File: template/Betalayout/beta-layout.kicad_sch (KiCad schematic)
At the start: 0 parts

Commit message: Update footprint for SMD capacitor and crystals
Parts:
- added CN1: GSB343K331HR, User_Github:GSB343K331HR, symbol User:GSB343K331HR
- added R1: 1K, symbol User:R
- added U1: LM1117IMPX-3.3/NOPB, User:LM1117IMPX-3.3NOPB, symbol User:LM1117IMPX-3.3/NOPB
- added U2: STM32F103C8T6, User:STM32F103C8T6, symbol User:STM32F103C8T6

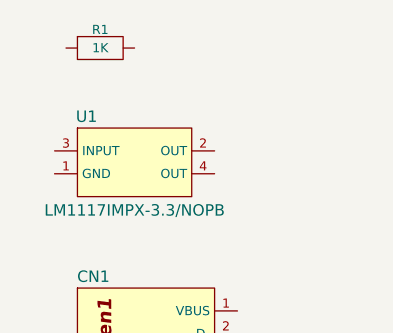
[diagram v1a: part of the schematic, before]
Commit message: Add footprint for SMD LED
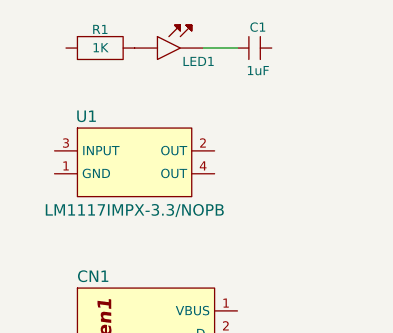
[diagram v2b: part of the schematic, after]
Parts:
- added C1: 1uF, symbol User:C
- added LED1: ~, symbol User:LED
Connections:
- net at R1.2: now also LED1.1
- new net: C1.1, LED1.2
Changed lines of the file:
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@@
 		(comment 1 "Zhangshun Lu")
+	)
+	(wire
+		(pts
+			(xy 38.1 25.4) (xy 34.29 25.4)
+		)
+		(stroke
+			(width 0)
+			(type default)
+		)
 	)
 	(symbol
@@
 	)
 	(symbol
+		(lib_id "User:LED")
+		(at 30.48 25.4 0)
+		(unit 1)
+		(exclude_from_sim no)
+		(in_bom yes)
+		(on_board yes)
+		(dnp no)
+		(fields_autoplaced yes)
+		(property "Reference" "LED1"
+			(at 33.782 26.924 0)
+			(do_not_autoplace yes)
+			(effects
+				(font
+					(size 1.016 1.016)
+				)
+			)
+		)
+		(property "Value" "~"
+			(at 30.48 25.4 0)
+			(do_not_autoplace yes)
+			(effects
+				(font
+					(size 1.016 1.016)
+					(color 64 55 255 1)
+				)
+				(hide yes)
+			)
+		)
+		(property "Footprint" ""
+			(at 30.48 25.4 0)
+			(effects
+				(font
+					(size 1.27 1.27)
+				)
+				(hide yes)
+			)
+		)
+		(property "Datasheet" ""
+			(at 30.48 25.4 0)
+			(effects
+				(font
+					(size 1.27 1.27)
+				)
+				(hide yes)
+			)
+		)
+		(property "Description" "LED"
+			(at 30.48 25.4 0)
+			(effects
+				(font
+					(size 1.27 1.27)
+				)
+				(hide yes)
+			)
+		)
+		(property "MPN" ""
+			(at 30.48 25.4 0)
+			(effects
+				(font
+					(size 1.016 1.016)
+				)
+				(hide yes)
+			)
+		)
+		(property "Manufacturer" ""
+			(at 30.48 25.4 0)
+			(effects
+				(font
+					(size 1.016 1.016)
+				)
+				(hide yes)
+			)
+		)
+		(pin "2"
+		)
+		(pin "1"
+		)
+		(instances
+			(project ""
+				(path "/695d78a6-3e90-439f-9889-ee1335c900cb"
+					(reference "LED1")
+					(unit 1)
+				)
+			)
+		)
+	)
+	(symbol
 		(lib_id "User:GSB343K331HR")
 		(at 27.94 49.53 0)
@@
 					(unit 1)
 				)
+			)
+		)
+	)
+	(symbol
+		(lib_id "User:C")
+		(at 40.64 25.4 0)
+		(unit 1)
+		(exclude_from_sim no)
+		(in_bom yes)
+		(on_board yes)
+		(dnp no)
+		(fields_autoplaced yes)
+		(property "Reference" "C1"
+			(at 40.386 23.114 0)
+			(do_not_autoplace yes)
+			(effects
+				(font
+					(size 1.016 1.016)
+				)
+			)
+		)
+		(property "Value" "1uF"
+			(at 40.386 27.94 0)
+			(do_not_autoplace yes)
+			(effects
+				(font
+					(size 1.016 1.016)
+					(color 64 55 255 1)
+				)
+			)
+		)
+		(property "Footprint" ""
+			(at 40.64 25.4 0)
+			(effects
+				(font
+					(size 1.27 1.27)
+				)
+				(hide yes)
+			)
+		)
+		(property "Datasheet" ""
+			(at 40.64 25.4 0)
+			(effects
+				(font
+					(size 1.27 1.27)
+				)
+				(hide yes)
+			)
+		)
+		(property "Description" "Capacitor"
+			(at 40.64 25.4 0)
+			(effects
+				(font
+					(size 1.27 1.27)
+				)
+				(hide yes)
+			)
+		)
+		(property "MPN" ""
+			(at 40.64 25.4 0)
+			(effects
+				(font
+					(size 1.016 1.016)
+				)
+				(hide yes)
+			)
+		)
+		(property "Manufacturer" ""
+			(at 40.64 25.4 0)
+			(effects
+				(font
+					(size 1.016 1.016)
+				)
+				(hide yes)
+			)
+		)
+		(pin "1"
+		)
+		(pin "2"
+		)
+		(instances
+			(project ""
+				(path "/695d78a6-3e90-439f-9889-ee1335c900cb"
+					(reference "C1")
+					(unit 1)
+				)

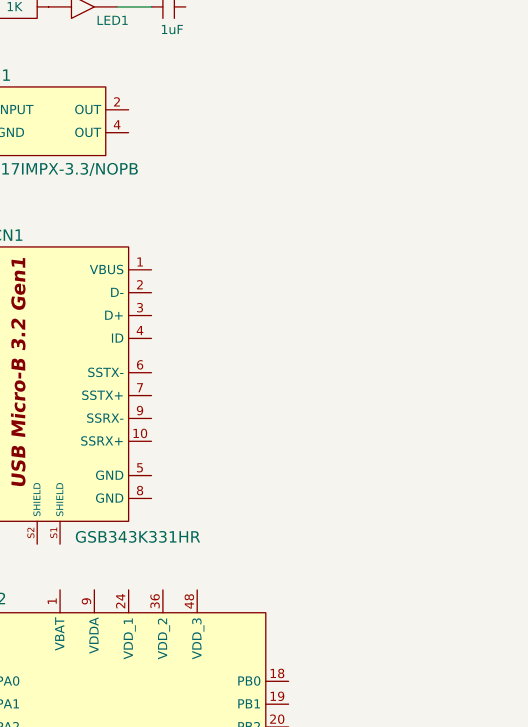
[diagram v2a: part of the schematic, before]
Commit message: Update footprint for USB2.0 type C recptacle
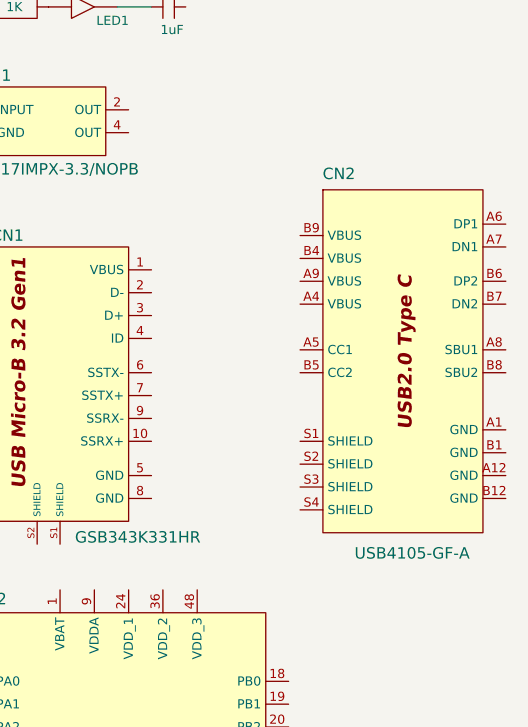
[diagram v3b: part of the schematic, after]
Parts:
- added CN2: USB4105-GF-A, User:USB4105-GF-A, symbol User:USB4105-GF-A
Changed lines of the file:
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@@
+	)
+	(symbol
+		(lib_id "User:USB4105-GF-A")
+		(at 66.04 46.99 0)
+		(unit 1)
+		(exclude_from_sim no)
+		(in_bom yes)
+		(on_board yes)
+		(dnp no)
+		(fields_autoplaced yes)
+		(property "Reference" "CN2"
+			(at 58.928 43.942 0)
+			(do_not_autoplace yes)
+			(effects
+				(font
+					(size 1.27 1.27)
+				)
+			)
+		)
+		(property "Value" "USB4105-GF-A"
+			(at 67.056 86.106 0)
+			(do_not_autoplace yes)
+			(effects
+				(font
+					(size 1.27 1.27)
+				)
+			)
+		)
+		(property "Footprint" "User:USB4105-GF-A"
+			(at 66.04 46.99 0)
+			(effects
+				(font
+					(size 1.27 1.27)
+				)
+				(hide yes)
+			)
+		)
+		(property "Datasheet" "https://www.digikey.de/en/products/detail/gct/USB4105-GF-A/11198441"
+			(at 66.04 46.99 0)
+			(effects
+				(font
+					(size 1.27 1.27)
+				)
+				(hide yes)
+			)
+		)
+		(property "Description" "USB2.0 TYP C"
+			(at 66.04 46.99 0)
+			(effects
+				(font
+					(size 1.27 1.27)
+				)
+				(hide yes)
+			)
+		)
+		(property "MPN" "USB4105-GF-A"
+			(at 66.04 46.99 0)
+			(effects
+				(font
+					(size 1.016 1.016)
+				)
+				(hide yes)
+			)
+		)
+		(property "Manufacturer" "GCT"
+			(at 66.04 46.99 0)
+			(effects
+				(font
+					(size 1.016 1.016)
+				)
+				(hide yes)
+			)
+		)
+		(pin "B4"
+		)
+		(pin "S1"
+		)
+		(pin "A9"
+		)
+		(pin "S3"
+		)
+		(pin "B6"
+		)
+		(pin "A8"
+		)
+		(pin "S2"
+		)
+		(pin "B5"
+		)
+		(pin "S4"
+		)
+		(pin "B7"
+		)
+		(pin "B1"
+		)
+		(pin "B9"
+		)
+		(pin "A7"
+		)
+		(pin "B8"
+		)
+		(pin "A1"
+		)
+		(pin "B12"
+		)
+		(pin "A4"
+		)
+		(pin "A5"
+		)
+		(pin "A6"
+		)
+		(pin "A12"
+		)
+		(instances
+			(project ""
+				(path "/695d78a6-3e90-439f-9889-ee1335c900cb"
+					(reference "CN2")
+					(unit 1)
+				)
+			)
+		)
 	)
 	(symbol

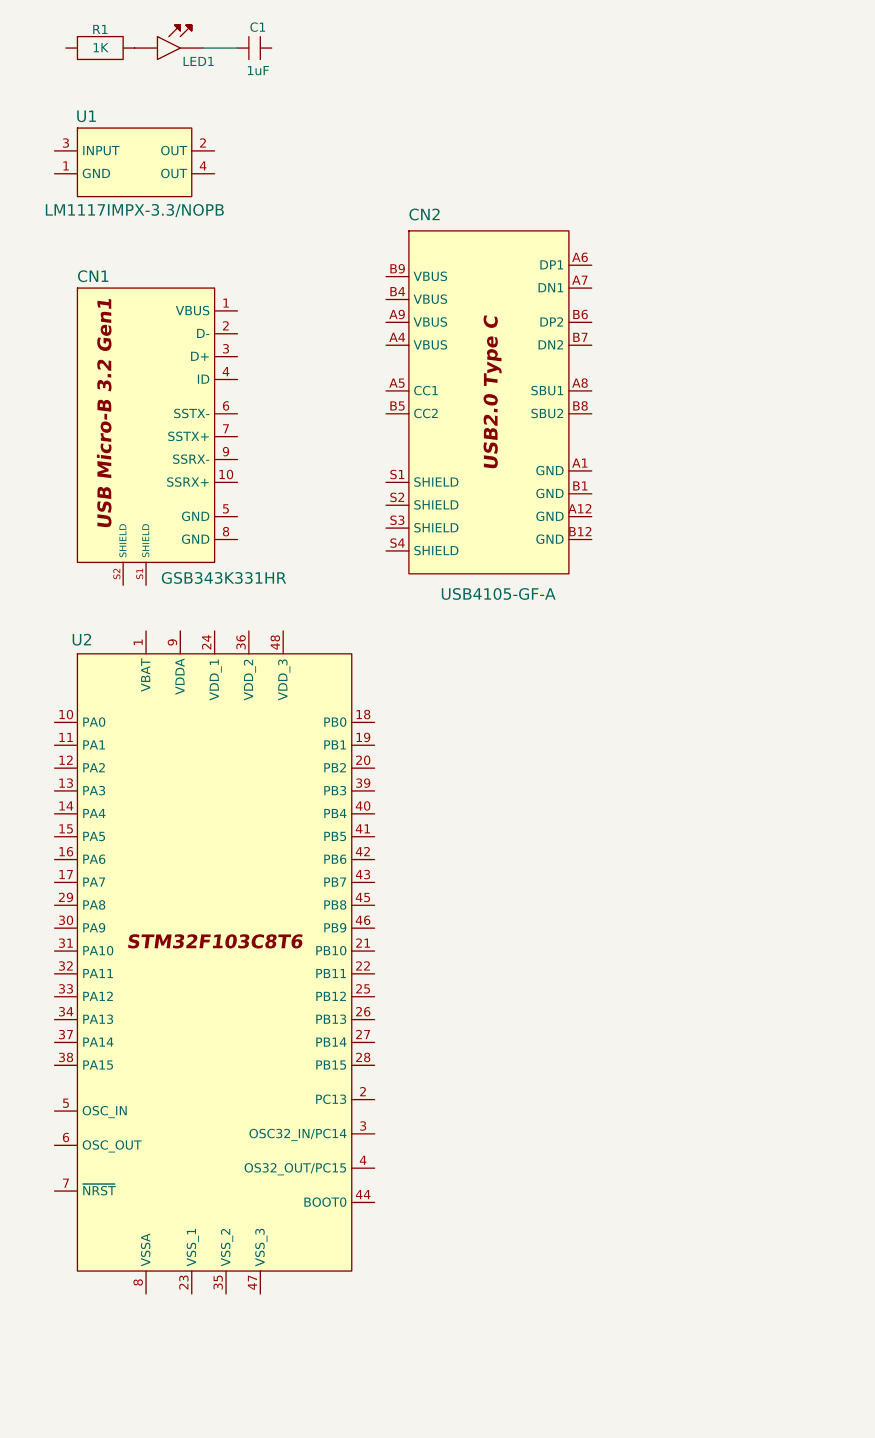
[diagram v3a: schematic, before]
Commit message: Add USB5744
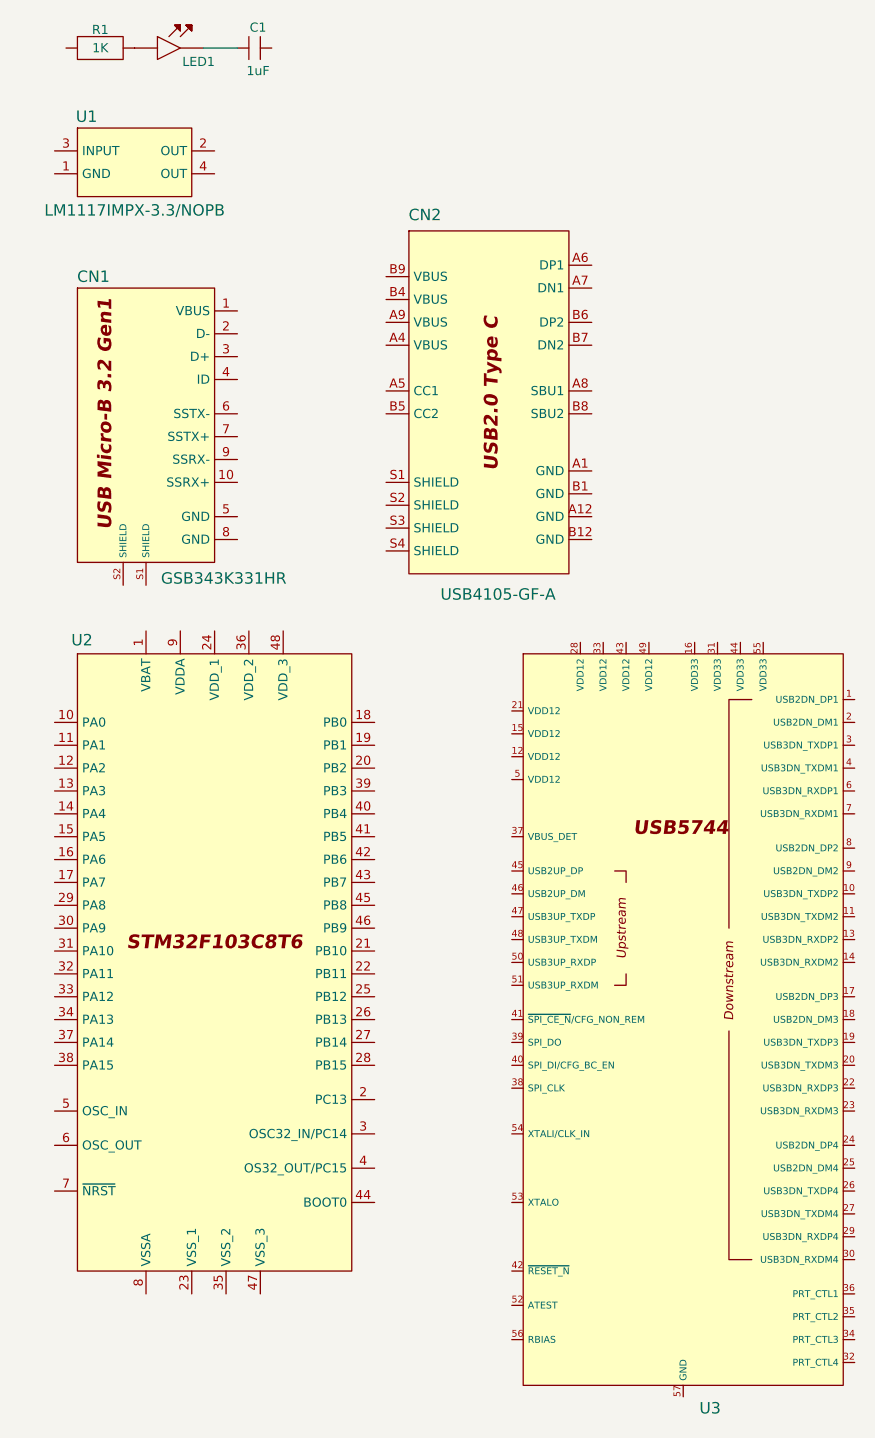
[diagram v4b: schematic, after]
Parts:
- added U3: USB5744, User:USB5744, symbol User:USB5744
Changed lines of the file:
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@@
+	)
+	(symbol
+		(lib_id "User:USB5744")
+		(at 87.63 105.41 0)
+		(unit 1)
+		(exclude_from_sim no)
+		(in_bom yes)
+		(on_board yes)
+		(dnp no)
+		(fields_autoplaced yes)
+		(property "Reference" "U3"
+			(at 89.4241 176.53 0)
+			(effects
+				(font
+					(size 1.27 1.27)
+				)
+				(justify left)
+			)
+		)
+		(property "Value" "USB5744"
+			(at 87.376 108.204 0)
+			(effects
+				(font
+					(size 1.27 1.27)
+				)
+				(hide yes)
+			)
+		)
+		(property "Footprint" "User:USB5744"
+			(at 85.344 83.058 0)
+			(effects
+				(font
+					(size 1.27 1.27)
+				)
+				(hide yes)
+			)
+		)
+		(property "Datasheet" "https://www.digikey.de/en/products/detail/microchip-technology/USB5744-2G/5323585"
+			(at 85.852 81.28 0)
+			(effects
+				(font
+					(size 1.27 1.27)
+				)
+				(hide yes)
+			)
+		)
+		(property "Description" "IC HUB CTLR USB 56VQFN"
+			(at 87.63 86.868 0)
+			(effects
+				(font
+					(size 1.27 1.27)
+				)
+				(hide yes)
+			)
+		)
+		(property "MPN" "USB5744/2G"
+			(at 86.36 86.868 0)
+			(effects
+				(font
+					(size 1.016 1.016)
+				)
+				(hide yes)
+			)
+		)
+		(property "Manufacturer" "Microchip Technology"
+			(at 86.868 86.868 0)
+			(effects
+				(font
+					(size 1.016 1.016)
+				)
+				(hide yes)
+			)
+		)
+		(pin "39"
+		)
+		(pin "49"
+		)
+		(pin "15"
+		)
+		(pin "38"
+		)
+		(pin "21"
+		)
+		(pin "40"
+		)
+		(pin "42"
+		)
+		(pin "5"
+		)
+		(pin "52"
+		)
+		(pin "45"
+		)
+		(pin "51"
+		)
+		(pin "28"
+		)
+		(pin "43"
+		)
+		(pin "10"
+		)
+		(pin "6"
+		)
+		(pin "50"
+		)
+		(pin "37"
+		)
+		(pin "46"
+		)
+		(pin "48"
+		)
+		(pin "12"
+		)
+		(pin "41"
+		)
+		(pin "54"
+		)
+		(pin "47"
+		)
+		(pin "53"
+		)
+		(pin "56"
+		)
+		(pin "33"
+		)
+		(pin "16"
+		)
+		(pin "31"
+		)
+		(pin "44"
+		)
+		(pin "55"
+		)
+		(pin "57"
+		)
+		(pin "1"
+		)
+		(pin "2"
+		)
+		(pin "4"
+		)
+		(pin "3"
+		)
+		(pin "7"
+		)
+		(pin "8"
+		)
+		(pin "9"
+		)
+		(pin "26"
+		)
+		(pin "14"
+		)
+		(pin "27"
+		)
+		(pin "32"
+		)
+		(pin "24"
+		)
+		(pin "17"
+		)
+		(pin "11"
+		)
+		(pin "13"
+		)
+		(pin "18"
+		)
+		(pin "19"
+		)
+		(pin "20"
+		)
+		(pin "25"
+		)
+		(pin "29"
+		)
+		(pin "22"
+		)
+		(pin "23"
+		)
+		(pin "36"
+		)
+		(pin "35"
+		)
+		(pin "30"
+		)
+		(pin "34"
+		)
+		(instances
+			(project ""
+				(path "/695d78a6-3e90-439f-9889-ee1335c900cb"
+					(reference "U3")
+					(unit 1)
+				)
+			)
+		)
 	)
 	(symbol
